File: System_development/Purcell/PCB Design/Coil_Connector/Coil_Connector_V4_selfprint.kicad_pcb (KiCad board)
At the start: 2 copper layers, 15.5 x 26.7 mm, 4 parts, among them J1 Conn_Coaxial

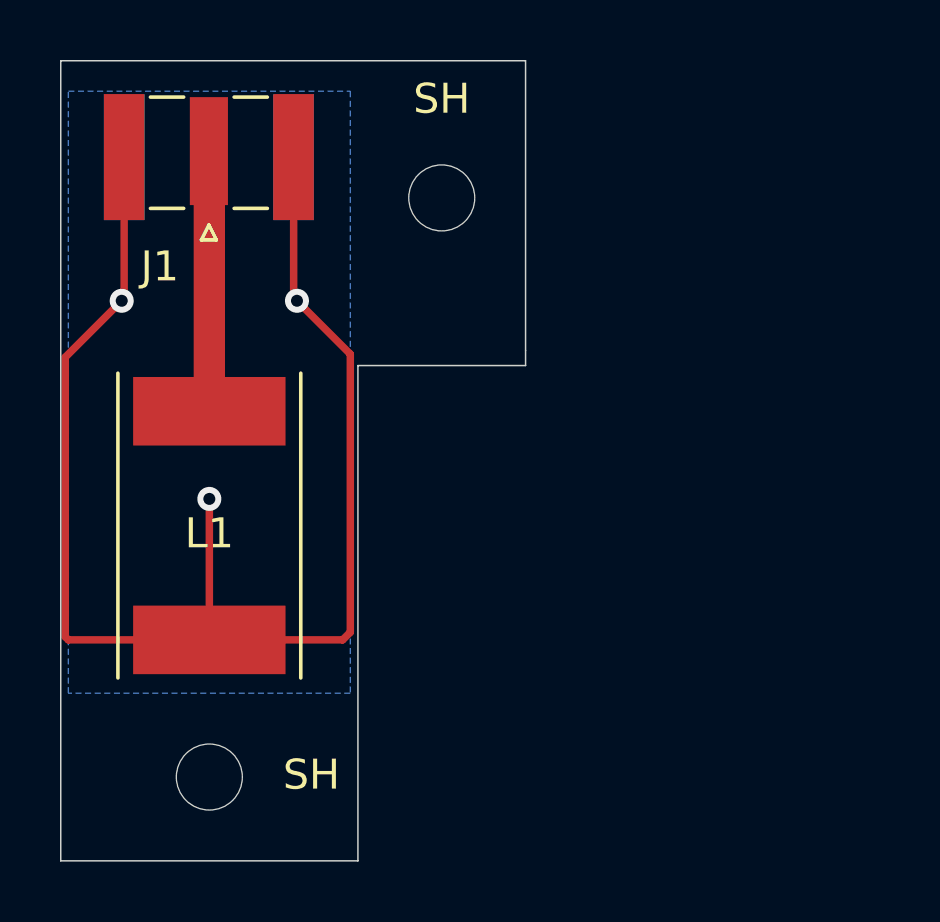
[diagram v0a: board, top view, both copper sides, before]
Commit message: Coil Connector V4
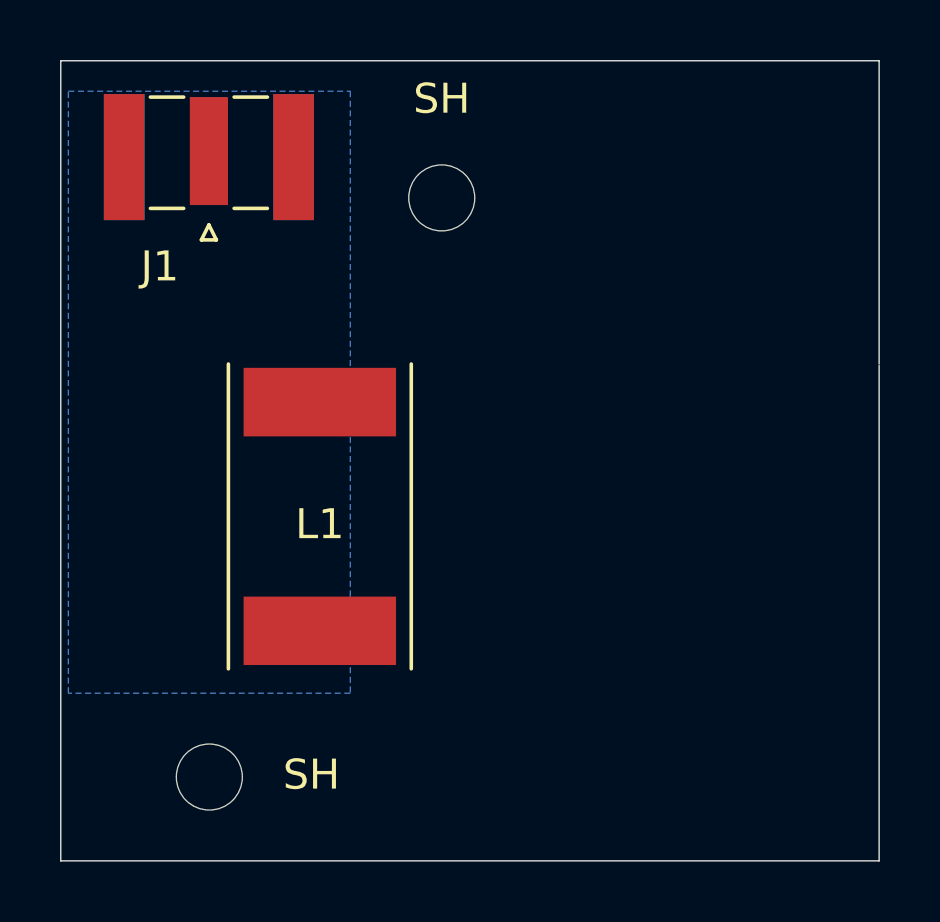
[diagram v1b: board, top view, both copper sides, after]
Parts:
- moved L1 3.70 mm to (142.7, 109.2)
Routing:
- net GND: track 49.2 -> 0.00 mm, vias 3 -> 0
- net Net-(J1-Pad1): track 6.98 -> 0.00 mm
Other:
- board size 15.5 x 26.7 mm -> 27.3 x 26.7 mm
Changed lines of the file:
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@@
 	(footprint "L_Coil:L_Coil"
 		(layer "F.Cu")
-		(at 139.065 109.474 180)
+		(at 142.748 109.1692 180)
 		(property "Reference" "L1"
 			(at 0 -3.056 0)
@@
 	)
 	(gr_line
-		(start 149.606 96.774)
-		(end 149.606 106.426)
-		(stroke
-			(width 0.05)
-			(type solid)
-		)
-		(layer "Edge.Cuts")
-	)
-	(gr_line
-		(start 149.606 106.426)
-		(end 149.606 106.934)
-		(stroke
-			(width 0.05)
-			(type solid)
-		)
-		(layer "Edge.Cuts")
-	)
-	(gr_line
-		(start 144.018 106.934)
-		(end 144.018 123.444)
+		(start 161.3916 96.774)
+		(end 161.3916 106.8832)
+		(stroke
+			(width 0.05)
+			(type solid)
+		)
+		(layer "Edge.Cuts")
+	)
+	(gr_line
+		(start 161.3916 106.934)
+		(end 161.3916 123.444)
 		(stroke
 			(width 0.05)
@@
 	(gr_line
 		(start 134.112 96.774)
-		(end 149.606 96.774)
-		(stroke
-			(width 0.05)
-			(type solid)
-		)
-		(layer "Edge.Cuts")
-	)
-	(gr_line
-		(start 144.018 123.444)
+		(end 161.3916 96.774)
+		(stroke
+			(width 0.05)
+			(type solid)
+		)
+		(layer "Edge.Cuts")
+	)
+	(gr_line
+		(start 161.3916 123.444)
 		(end 134.112 123.444)
-		(stroke
-			(width 0.05)
-			(type solid)
-		)
-		(layer "Edge.Cuts")
-	)
-	(gr_line
-		(start 149.606 106.934)
-		(end 144.018 106.934)
 		(stroke
 			(width 0.05)
@@
 		(layer "Edge.Cuts")
 	)
-	(segment
-		(start 139.065 111.379)
-		(end 139.065 116.078)
-		(width 0.25)
-		(layer "F.Cu")
-		(net 1)
-	)
-	(segment
-		(start 136.225 99.9855)
-		(end 136.225 104.694)
-		(width 0.25)
-		(layer "F.Cu")
-		(net 1)
-	)
-	(segment
-		(start 141.875 99.9855)
-		(end 141.875 104.664)
-		(width 0.25)
-		(layer "F.Cu")
-		(net 1)
-	)
-	(segment
-		(start 134.366 116.078)
-		(end 134.262 115.974)
-		(width 0.25)
-		(layer "F.Cu")
-		(net 1)
-	)
-	(segment
-		(start 136.225 104.694)
-		(end 136.144 104.775)
-		(width 0.25)
-		(layer "F.Cu")
-		(net 1)
-	)
-	(segment
-		(start 136.144 104.775)
-		(end 134.262 106.657)
-		(width 0.25)
-		(layer "F.Cu")
-		(net 1)
-	)
-	(segment
-		(start 134.262 106.657)
-		(end 134.262 115.974)
-		(width 0.25)
-		(layer "F.Cu")
-		(net 1)
-	)
-	(segment
-		(start 141.986 104.775)
-		(end 143.764 106.553)
-		(width 0.25)
-		(layer "F.Cu")
-		(net 1)
-	)
-	(segment
-		(start 140.462 116.078)
-		(end 139.065 116.078)
-		(width 0.25)
-		(layer "F.Cu")
-		(net 1)
-	)
-	(segment
-		(start 139.065 116.078)
-		(end 143.51 116.078)
-		(width 0.25)
-		(layer "F.Cu")
-		(net 1)
-	)
-	(segment
-		(start 143.764 106.553)
-		(end 143.764 115.824)
-		(width 0.25)
-		(layer "F.Cu")
-		(net 1)
-	)
-	(segment
-		(start 143.51 116.078)
-		(end 143.764 115.824)
-		(width 0.25)
-		(layer "F.Cu")
-		(net 1)
-	)
-	(segment
-		(start 141.875 104.664)
-		(end 141.986 104.775)
-		(width 0.25)
-		(layer "F.Cu")
-		(net 1)
-	)
-	(segment
-		(start 139.065 116.078)
-		(end 134.366 116.078)
-		(width 0.25)
-		(layer "F.Cu")
-		(net 1)
-	)
-	(via
-		(at 141.986 104.775)
-		(size 0.8)
-		(drill 0.4)
-		(layers "F.Cu" "B.Cu")
-		(free yes)
-		(net 1)
-	)
-	(via
-		(at 136.144 104.775)
-		(size 0.8)
-		(drill 0.4)
-		(layers "F.Cu" "B.Cu")
-		(free yes)
-		(net 1)
-	)
-	(via
-		(at 139.065 111.379)
-		(size 0.8)
-		(drill 0.4)
-		(layers "F.Cu" "B.Cu")
-		(free yes)
-		(net 1)
-	)
-	(segment
-		(start 139.065 101.473)
-		(end 139.065 108.458)
-		(width 1.044)
-		(layer "F.Cu")
-		(net 2)
-	)
 	(zone
